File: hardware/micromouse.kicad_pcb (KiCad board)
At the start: 2 copper layers, 109 x 74 mm, 92 parts, among them CN1 5_PIN_HEADER, CN2 5_PIN_HEADER, J1 uSD_SLOT_47219-2001, M1 MOTOR_MOUNTS_AND_ENCODERS, M2 JST_CONNECTOR_FEMALE.-THROUGH, M3 2.54MM-SLIDE-SWITCH_TS02_SWIT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, SW1 SWITCH_DPST, SW2 SWITCH_DPST, SW3 SWITCH_DPST, U1 STM32F446RE_LQFP64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

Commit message: PCB updated
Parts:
- removed LED_BLUE1, LED_BLUE2, LED_BLUE3, LED_BLUE4, LED_GREEN1, LED_GREEN3, LED_GREEN4, LED_RED2, LED_RED3: Led_Small, LEDs:LED_0603
- removed R1, R10, R11, R2, R3, R6, R7, R8, R9: 1k, footprints_micromouse:R_0603_HandSoldering
- moved R_BOOT1 1.71 mm to (170.0, 76.3)
- moved CN2 1.00 mm to (176.0, 120.0)
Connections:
- U1 pad PA7: LED5 -> Net-(U1-PadPA7)
- U1 pad PB0: LED8 -> Net-(U1-PadPB0)
- U1 pad PC1: LED0 -> Net-(U1-PadPC1)
- U1 pad PC2: LED1 -> Net-(U1-PadPC2)
- U1 pad PC3: LED2 -> Net-(U1-PadPC3)
- U1 pad PC4: LED6 -> Net-(U1-PadPC4)
- U1 pad PC5: LED7 -> Net-(U1-PadPC5)
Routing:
- net GND: track 343.4 -> 437.8 mm, vias 22 -> 33
- net VOL_METER: track 2.41 -> 84.7 mm, vias 0 -> 4
- net (no net): track 0.00 -> 72.5 mm, vias 0 -> 9
- net ROT_L_CHB: track 0.00 -> 70.5 mm, vias 0 -> 4
- net PB2: track 12.2 -> 77.5 mm, vias 0 -> 4
- net SWDIO: track 0.00 -> 52.3 mm, vias 0 -> 2
- net SWCLK: track 0.00 -> 51.6 mm, vias 0 -> 1
- net +3V3: track 422.8 -> 468.3 mm, vias 19 -> 23
- net IMU_INT: track 0.00 -> 40.3 mm, vias 0 -> 4
- net RESET: track 116.8 -> 153.7 mm, vias 2 -> 3
- net USART_RX: track 0.00 -> 33.7 mm, vias 0 -> 3
- net +BATT: track 137.0 -> 169.5 mm, vias 0 -> 3
- net IMU_SDA: track 1.81 -> 29.6 mm, vias 0 -> 2
- net +5V: track 191.1 -> 218.7 mm
- net DIS_MOSI: track 0.00 -> 27.3 mm, vias 0 -> 1
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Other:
- outline, holes or cut-outs redrawn

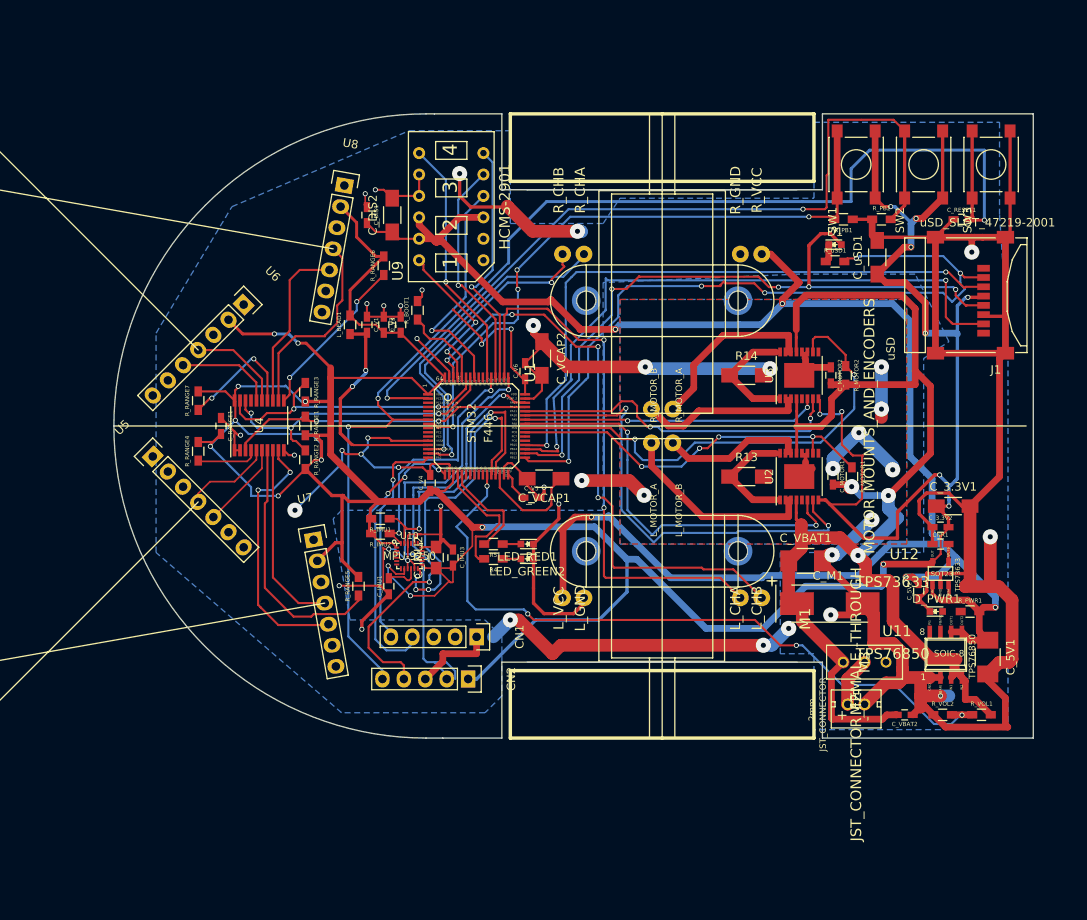
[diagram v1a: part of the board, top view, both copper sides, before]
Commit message: PCB board- needs to check the motor driver
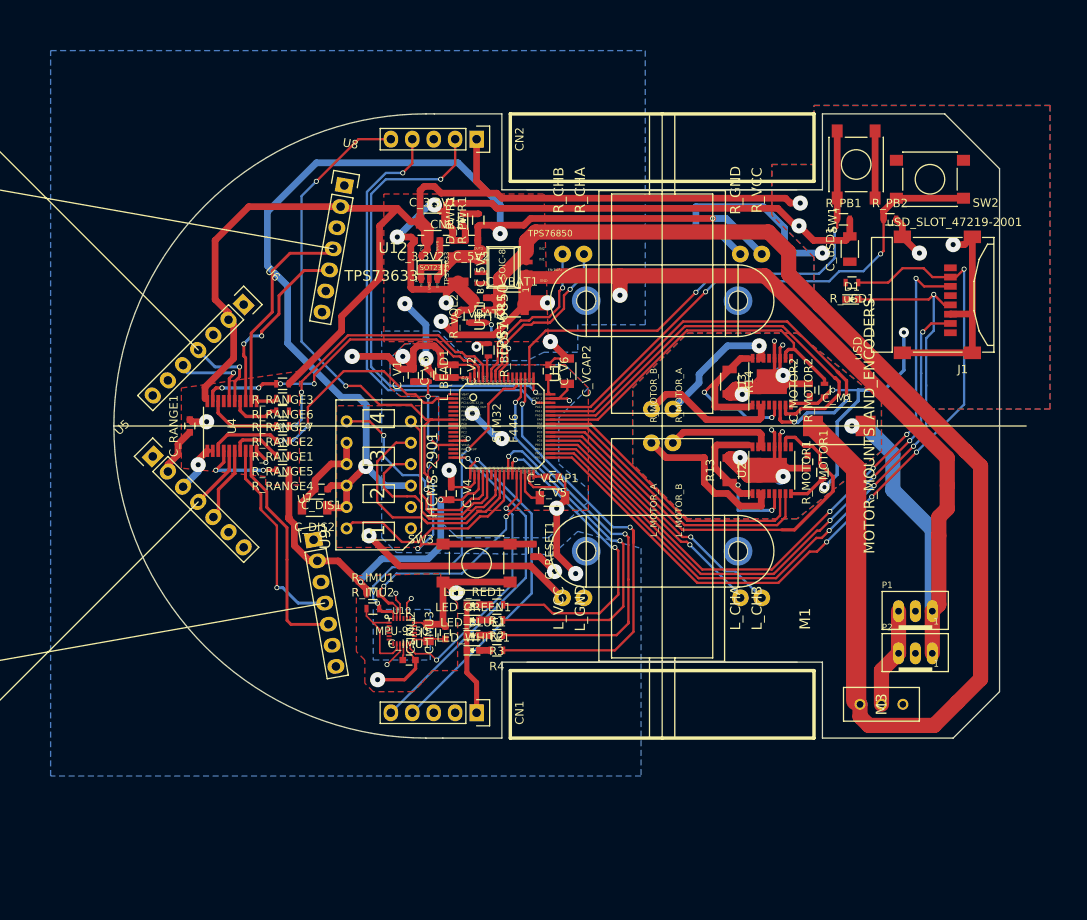
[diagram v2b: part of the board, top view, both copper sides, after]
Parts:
- removed LED_GREEN2: Led_Small, LEDs:LED_0603
- removed M2: JST_CONNECTOR_FEMALE.-THROUGH, pcb1:JST_CONNECTOR_FEMALE.-THROUGH-HOLE_JST_CONNECTOR_FEMALE
- removed R5: 1k, footprints_micromouse:R_0603_HandSoldering
- added LED_BLUE1: Led_Small, LEDs:LED_0603, F.Cu at (176.6, 114.8)
- added LED_GREEN1: Led_Small, LEDs:LED_0603, F.Cu at (176.6, 113.0)
- added LED_WHITE1: Led_Small, LEDs:LED_0603, F.Cu at (176.6, 116.6)
- added P1: B3B-PH-SM4-TB, footprints_micromouse:JST_B3B-PH_HEADER, F.Cu at (229.0, 112.0)
- added P2: B3B-PH-SM4-TB, footprints_micromouse:JST_B3B-PH_HEADER, F.Cu at (229.0, 117.0)
- added R1: 1k, Resistors_SMD:R_0603, F.Cu at (179.4, 111.2)
- added R2: 1k, Resistors_SMD:R_0603, F.Cu at (179.4, 113.0)
- added R3: 1k, Resistors_SMD:R_0603, F.Cu at (179.4, 114.8)
- CNR1, C_3.3V2, C_5V2, C_DIS1, C_IMU1, C_IMU3, C_MOTOR1, C_MOTOR2, C_RANGE1, C_RESET1, C_V1, C_V2, C_V3, C_V4, C_V5, C_V6, C_VBAT2: footprint footprints_micromouse:C_0603_HandSoldering -> Capacitors_SMD:C_0603
- C_3.3V1, C_DIS2, C_VCAP1, C_VCAP2, C_uSD1: footprint Capacitors_SMD:C_1206_HandSoldering -> Capacitors_SMD:C_1206
- C_5V1, C_VBAT1: footprint Capacitors_SMD:C_1210_HandSoldering -> Capacitors_SMD:C_1210
- C_IMU2: footprint Capacitors_SMD:C_0805_HandSoldering -> Capacitors_SMD:C_0805
- C_M1: footprint Capacitors_Tantalum_SMD:TantalC_SizeD_EIA-7343_HandSoldering -> Capacitors_Tantalum_SMD:TantalC_SizeD_EIA-7343_Reflow
- L_BEAD1, R4, R_BOOT1, R_IMU1, R_IMU2, R_MOTOR1, R_MOTOR2, R_PB1, R_PB2, R_PWR1, R_RANGE1, R_RANGE2, R_RANGE3, R_RANGE4, R_RANGE5, R_RANGE6, R_RANGE7, R_VOL1, R_VOL2, R_uSD1: footprint footprints_micromouse:R_0603_HandSoldering -> Resistors_SMD:R_0603
- R13, R14: footprint Resistors_SMD:R_1206_HandSoldering -> Resistors_SMD:R_1206
- moved C_5V1 77.8 mm to (174.8, 71.4)
- moved SW3 77.2 mm to (177.0, 106.2), turned to 0 degrees
- moved R_VOL1 75.5 mm to (178.0, 77.0), turned to 270 degrees
- moved R_PWR1 74.5 mm to (177.2, 65.6), turned to 90 degrees
- moved R_VOL2 73.3 mm to (176.2, 77.0), turned to 90 degrees
- moved D_PWR1 72.8 mm to (175.4, 65.6), turned to 90 degrees
- moved U12 70.6 mm to (171.4, 71.2)
- moved C_VBAT2 70.6 mm to (177.4, 74.8), turned to 180 degrees
- moved C_3.3V2 70.4 mm to (170.4, 68.0)
- moved C_3.3V1 70.3 mm to (171.8, 65.8)
- moved U11 69.7 mm to (180.2, 71.2), turned to 90 degrees
- moved CNR1 68.8 mm to (173.4, 68.0), turned to 0 degrees
- moved C_5V2 67.4 mm to (176.4, 68.0), turned to 180 degrees
- moved C_RESET1 64.2 mm to (183.8, 104.8), turned to 270 degrees
- moved CN2 64.0 mm to (177.0, 56.0)
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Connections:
- R4 pad 1: LED3 -> LED4
- R_MOTOR1 pad 1: +BATT -> +3V3
- R_MOTOR2 pad 1: +BATT -> +3V3
- R_PB1 pad 1: PB2 -> PB1
- R_PB2 pad 1: PB1 -> PB2
- SW1 pad 1: PB2 -> PB1
- SW2 pad 1: PB1 -> PB2
- U1 pad PA0_: ROT_R_CHA -> Net-(U1-PadPA0_)
- U1 pad PA1: ROT_R_CHB -> Net-(U1-PadPA1)
- U1 pad PA10: MOTOR_L_DIR -> MOTOR_R_DIR
- U1 pad PA11: MOTOR_R_DIR -> MOTOR_R_PWM
- U1 pad PA12: ~RANGE_RESET -> PB2
- U1 pad PA15: ROT_L_CHA -> PB1
- U1 pad PA4: LED3 -> ~DIS_CE
- U1 pad PA5: LED4 -> DIS_SCK
- U1 pad PA7: Net-(U1-PadPA7) -> DIS_MOSI
- U1 pad PA9: MOTOR_R_PWM -> ~MOTOR_R_FAULT
- U1 pad PB0: Net-(U1-PadPB0) -> LED2
- U1 pad PB1: VOL_METER -> LED1
- U1 pad PB5: DIS_MOSI -> VOL_METER
- U1 pad PB6: RANGE_SCL -> ROT_R_CHA
- U1 pad PB7: RANGE_SDA -> ROT_R_CHB
- U1 pad PB8: ~DIS_RESET -> RANGE_SCL
- U1 pad PB9: ROT_L_CHB -> RANGE_SDA
- U1 pad PC0: PB2 -> Net-(U1-PadPC0)
- U1 pad PC10: DIS_SCK -> LED4
- U1 pad PC11: DIS_RS -> LED3
- U1 pad PC13: PB1 -> ~RANGE_RESET
- U1 pad PC4: Net-(U1-PadPC4) -> DIS_RS
- U1 pad PC5: Net-(U1-PadPC5) -> ~DIS_RESET
- U1 pad PC6: LED9 -> ROT_L_CHA
- U1 pad PC7: LED10 -> ROT_L_CHB
- U1 pad PC9: ~MOTOR_R_FAULT -> MOTOR_L_DIR
- U1 pad PD2: ~DIS_CE -> Net-(U1-PadPD2)
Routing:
- net +3V3: track 468.3 -> 267.8 mm, vias 23 -> 8
- net VOL_METER: track 84.7 -> 10.2 mm, vias 4 -> 2
- net RESET: track 153.7 -> 83.5 mm, vias 3 -> 4
- net (no net): track 72.5 -> 4.74 mm, vias 9 -> 2
- net +5V: track 218.7 -> 167.0 mm, vias 5 -> 4
- net GND: track 437.8 -> 481.9 mm, vias 33 -> 37
- net LED2: track 0.00 -> 42.9 mm, vias 0 -> 2
- net LED4: track 12.4 -> 54.7 mm, vias 0 -> 2
- net PB1: track 98.3 -> 59.4 mm
- net LED1: track 0.00 -> 38.7 mm, vias 0 -> 2
- net ROT_L_CHB: track 70.5 -> 33.0 mm, vias 4 -> 1
- net ROT_L_CHA: track 66.7 -> 30.4 mm, vias 2 -> 1
- net LED3: track 15.6 -> 51.3 mm, vias 0 -> 2
- net Net-(R_RANGE5-Pad2): track 30.3 -> 6.17 mm
- net MOTOR_R_PWM: track 35.2 -> 55.6 mm
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- added copper zone on F.Cu, net +3V3
- added copper zone on F.Cu, net +5V
- added copper zone on F.Cu, net +BATT
- removed copper zone on F.Cu, net GND
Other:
- board size 109 x 74 mm -> 105 x 74 mm
- net class Default: clearance 0.16 -> 0.15
- net class Thick added: clearance 0.3, trace_width 0.25, via_dia 0.6, via_drill 0.4
- rule trace_clearance: 0.16 -> 0.15

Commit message: Finished the PCB
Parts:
- U2, U3: footprint Housings_SSOP:TSSOP-16-1EP_4.4x5mm_Pitch0.65mm -> footprints_micromouse:TSSOP-16_EP
- moved M3 1.00 mm to (225.0, 122.0)
- moved P1 1.00 mm to (229.0, 111.0)
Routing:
- net GND: track 481.9 -> 508.1 mm
- net +BATT: track 160.3 -> 175.4 mm, vias 0 -> 3
- net (no net): track 4.74 -> 0.65 mm, vias 2 -> 0
- net Net-(D1-Pad1): track 0.00 -> 2.00 mm
- net SWDIO: track 54.1 -> 55.5 mm
- net LED4: track 54.7 -> 56.0 mm
- net LED3: track 51.3 -> 52.5 mm
- net +3V3: track 267.8 -> 268.8 mm
- net ~MOTOR_R_FAULT: track 42.1 -> 43.1 mm
- net Net-(R14-Pad1): track 25.8 -> 26.6 mm
- net IMU_SDA: track 42.0 -> 42.7 mm

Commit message: PCB Completed
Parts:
- CN1, CN2: footprint Pin_Headers:Pin_Header_Straight_1x05 -> footprints_micromouse:Pin_Header_Straight_1x05
- CNR1, C_3.3V2, C_5V2, C_DIS1, C_IMU1, C_IMU3, C_MOTOR1, C_MOTOR2, C_RANGE1, C_RESET1, C_V1, C_V2, C_V3, C_V4, C_V5, C_V6, C_VBAT2: footprint Capacitors_SMD:C_0603 -> footprints_micromouse:C_0603
- C_3.3V1, C_DIS2, C_VCAP1, C_VCAP2, C_uSD1: footprint Capacitors_SMD:C_1206 -> footprints_micromouse:C_1206
- C_5V1, C_VBAT1: footprint Capacitors_SMD:C_1210 -> footprints_micromouse:C_1210
- C_IMU2: footprint Capacitors_SMD:C_0805 -> footprints_micromouse:C_0805
- C_M1: footprint Capacitors_Tantalum_SMD:TantalC_SizeD_EIA-7343_Reflow -> footprints_micromouse:TantalC_SizeD_EIA-7343_Reflow
- D1, D_PWR1, LED_BLUE1, LED_GREEN1, LED_RED1, LED_WHITE1: footprint LEDs:LED_0603 -> footprints_micromouse:LED_0603
- L_BEAD1, R1, R2, R3, R4, R_BOOT1, R_IMU1, R_IMU2, R_MOTOR1, R_MOTOR2, R_PB1, R_PB2, R_PWR1, R_RANGE1, R_RANGE2, R_RANGE3, R_RANGE4, R_RANGE5, R_RANGE6, R_RANGE7, R_VOL1, R_VOL2, R_uSD1: footprint Resistors_SMD:R_0603 -> footprints_micromouse:R_0603
- R13, R14: footprint Resistors_SMD:R_1206 -> footprints_micromouse:R_1206
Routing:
- net +BATT: track 175.4 -> 173.9 mm
- net +5V: track 167.0 -> 168.3 mm
- net (no net): track 0.65 -> 0.00 mm
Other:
- board text added: "Designed by: Bumsik Kim"
- board text added: "WolfieMouse"

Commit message: Fixed for the PCB manufacturer requirements
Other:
- board size 105 x 74 mm -> 100 x 74 mm
